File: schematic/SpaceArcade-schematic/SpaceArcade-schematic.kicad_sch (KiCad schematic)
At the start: 4 parts, among them CON1 KY-023, M1 NEMA11

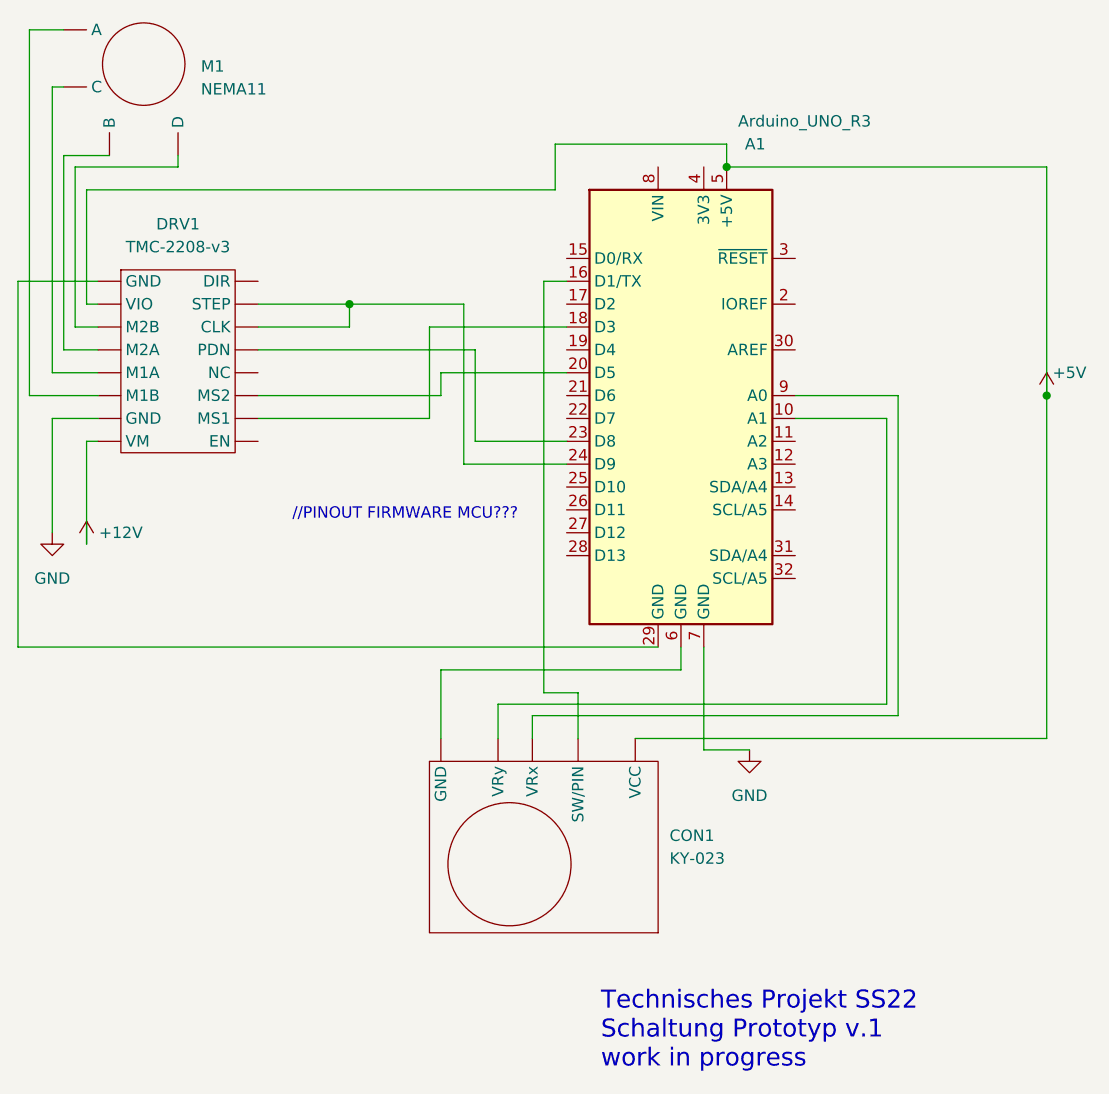
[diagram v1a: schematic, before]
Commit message: Fixing wiring
Fixing driver wiring
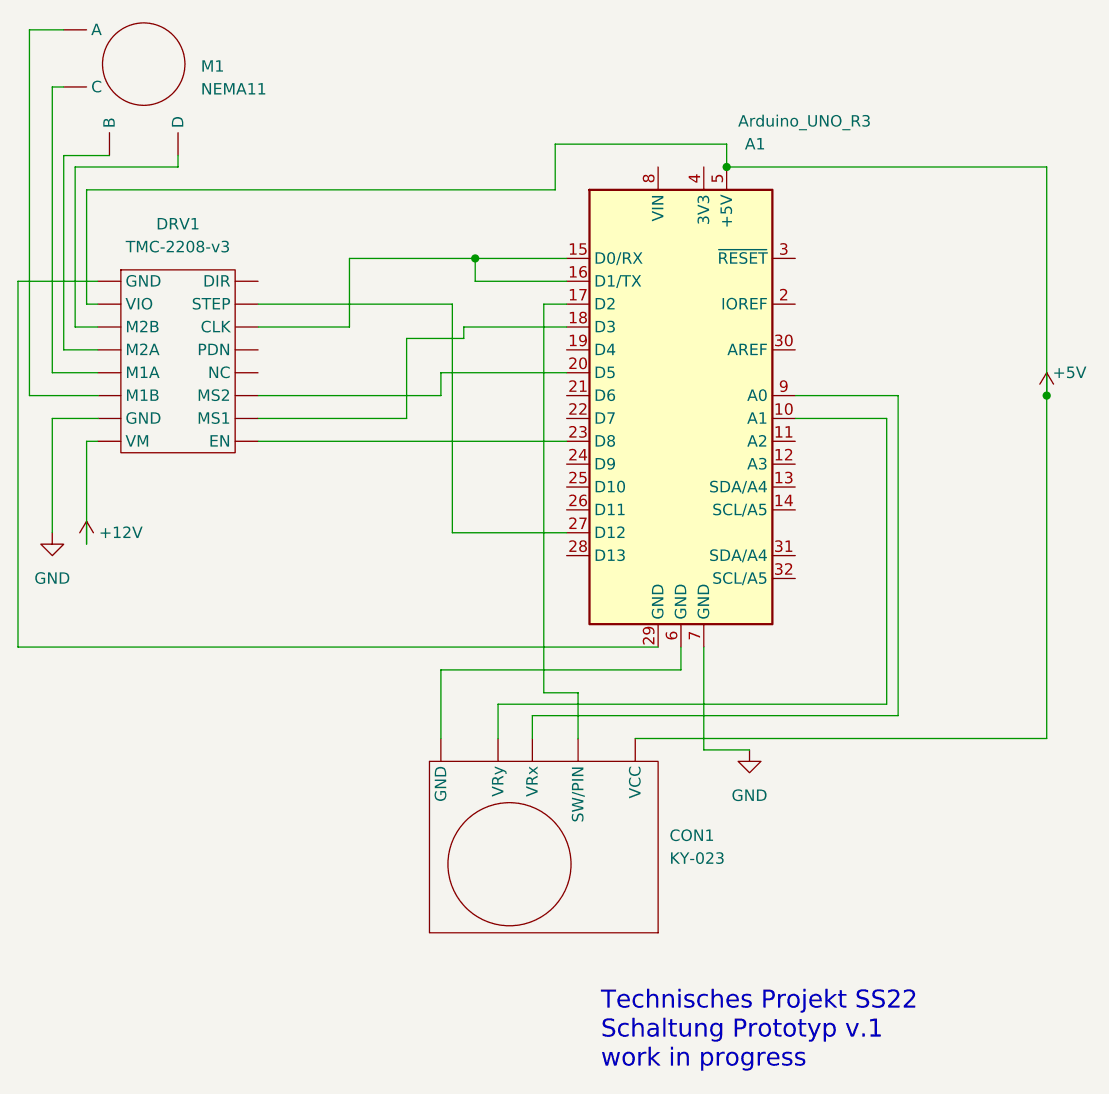
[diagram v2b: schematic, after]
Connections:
- net at A1.24 (D9): no longer DRV1. (VM)
- net at A1.15 (D0/RX): now also A1.16 (D1/TX), DRV1. (VM)
- net at A1.17 (D2): now also CON1. (VRy)
- net at A1.27 (D12): now also DRV1. (VM)
- new net: DRV1. (VM), M1. (D) (x3)
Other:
- note removed: "//PINOUT FIRMWARE MCU???"
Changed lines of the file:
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@@
   (junction (at 194.31 78.74) (diameter 0) (color 255 0 0 1)
   )
-  (junction (at 152.4 93.98) (diameter 0) (color 255 0 255 1)
+  (junction (at 166.37 88.9) (diameter 0) (color 0 0 0 0)
   )
   (junction (at 229.87 104.14) (diameter 0) (color 0 0 0 0)
@@
     (stroke (width 0) (type default) (color 0 0 0 1))
   )
-  (wire (pts (xy 142.24 99.06) (xy 166.37 99.06))
-    (stroke (width 0) (type default) (color 0 255 255 1))
-  )
   (wire (pts (xy 123.19 81.28) (xy 175.26 81.28))
     (stroke (width 0) (type default) (color 255 0 0 1))
@@
   (wire (pts (xy 212.09 106.68) (xy 201.93 106.68))
     (stroke (width 0) (type default) (color 132 0 132 1))
+  )
+  (wire (pts (xy 142.24 93.98) (xy 163.83 93.98))
+    (stroke (width 0) (type default) (color 0 0 0 0))
   )
   (wire (pts (xy 142.24 104.14) (xy 162.56 104.14))
     (stroke (width 0) (type default) (color 0 0 255 1))
   )
+  (wire (pts (xy 142.24 106.68) (xy 158.75 106.68))
+    (stroke (width 0) (type default) (color 0 255 255 1))
+  )
   (wire (pts (xy 120.65 63.5) (xy 116.84 63.5))
     (stroke (width 0) (type default) (color 255 153 0 1))
@@
     (stroke (width 0) (type default) (color 0 132 132 1))
   )
+  (wire (pts (xy 176.53 88.9) (xy 166.37 88.9))
+    (stroke (width 0) (type default) (color 0 0 0 0))
+  )
   (wire (pts (xy 213.36 104.14) (xy 201.93 104.14))
+    (stroke (width 0) (type default) (color 0 255 255 1))
+  )
+  (wire (pts (xy 165.1 97.79) (xy 165.1 96.52))
     (stroke (width 0) (type default) (color 0 255 255 1))
   )
@@
     (stroke (width 0) (type default) (color 0 0 255 1))
   )
-  (wire (pts (xy 152.4 93.98) (xy 142.24 93.98))
-    (stroke (width 0) (type default) (color 255 0 255 1))
+  (wire (pts (xy 165.1 96.52) (xy 176.53 96.52))
+    (stroke (width 0) (type default) (color 0 255 255 1))
   )
   (wire (pts (xy 213.36 139.7) (xy 213.36 104.14))
     (stroke (width 0) (type default) (color 0 255 255 1))
-  )
-  (wire (pts (xy 165.1 93.98) (xy 152.4 93.98))
-    (stroke (width 0) (type default) (color 255 0 255 1))
   )
   (wire (pts (xy 162.56 101.6) (xy 176.53 101.6))
@@
     (stroke (width 0) (type default) (color 255 0 0 1))
   )
+  (wire (pts (xy 176.53 93.98) (xy 173.99 93.98))
+    (stroke (width 0) (type default) (color 255 255 0 1))
+  )
   (wire (pts (xy 115.57 132.08) (xy 186.69 132.08))
     (stroke (width 0) (type default) (color 0 0 0 1))
@@
     (stroke (width 0) (type default) (color 255 0 0 1))
   )
+  (wire (pts (xy 158.75 106.68) (xy 158.75 97.79))
+    (stroke (width 0) (type default) (color 0 255 255 1))
+  )
+  (wire (pts (xy 166.37 88.9) (xy 152.4 88.9))
+    (stroke (width 0) (type default) (color 0 0 0 0))
+  )
+  (wire (pts (xy 166.37 88.9) (xy 166.37 91.44))
+    (stroke (width 0) (type default) (color 0 0 0 0))
+  )
   (wire (pts (xy 115.57 91.44) (xy 124.46 91.44))
     (stroke (width 0) (type default) (color 0 0 0 1))
   )
-  (wire (pts (xy 176.53 111.76) (xy 165.1 111.76))
-    (stroke (width 0) (type default) (color 255 0 255 1))
-  )
-  (wire (pts (xy 165.1 111.76) (xy 165.1 93.98))
-    (stroke (width 0) (type default) (color 255 0 255 1))
+  (wire (pts (xy 152.4 88.9) (xy 152.4 96.52))
+    (stroke (width 0) (type default) (color 0 0 0 0))
   )
   (wire (pts (xy 162.56 134.62) (xy 189.23 134.62))
     (stroke (width 0) (type default) (color 0 0 0 1))
   )
+  (wire (pts (xy 176.53 91.44) (xy 166.37 91.44))
+    (stroke (width 0) (type default) (color 0 0 0 0))
+  )
   (wire (pts (xy 172.72 139.7) (xy 213.36 139.7))
     (stroke (width 0) (type default) (color 0 255 255 1))
   )
+  (wire (pts (xy 152.4 96.52) (xy 142.24 96.52))
+    (stroke (width 0) (type default) (color 0 0 0 0))
+  )
+  (wire (pts (xy 163.83 93.98) (xy 163.83 119.38))
+    (stroke (width 0) (type default) (color 0 0 0 0))
+  )
   (wire (pts (xy 119.38 119.38) (xy 119.38 106.68))
     (stroke (width 0) (type default) (color 0 0 0 1))
+  )
+  (wire (pts (xy 163.83 119.38) (xy 176.53 119.38))
+    (stroke (width 0) (type default) (color 0 0 0 0))
   )
   (wire (pts (xy 124.46 99.06) (xy 120.65 99.06))
@@
     (stroke (width 0) (type default) (color 0 0 0 1))
   )
-  (wire (pts (xy 166.37 99.06) (xy 166.37 109.22))
-    (stroke (width 0) (type default) (color 0 255 255 1))
-  )
-  (wire (pts (xy 166.37 109.22) (xy 176.53 109.22))
-    (stroke (width 0) (type default) (color 0 255 255 1))
-  )
   (wire (pts (xy 120.65 77.47) (xy 120.65 99.06))
     (stroke (width 0) (type default) (color 0 0 0 0))
   )
-  (wire (pts (xy 161.29 96.52) (xy 176.53 96.52))
-    (stroke (width 0) (type default) (color 0 255 0 1))
-  )
-  (wire (pts (xy 142.24 106.68) (xy 161.29 106.68))
-    (stroke (width 0) (type default) (color 0 255 0 1))
-  )
-  (wire (pts (xy 161.29 106.68) (xy 161.29 96.52))
-    (stroke (width 0) (type default) (color 0 255 0 1))
+  (wire (pts (xy 142.24 109.22) (xy 176.53 109.22))
+    (stroke (width 0) (type default) (color 0 0 0 0))
   )
   (wire (pts (xy 121.92 96.52) (xy 121.92 78.74))
@@
     (stroke (width 0) (type default) (color 0 0 0 1))
   )
-  (wire (pts (xy 173.99 91.44) (xy 176.53 91.44))
-    (stroke (width 0) (type default) (color 255 255 0 1))
+  (wire (pts (xy 158.75 97.79) (xy 165.1 97.79))
+    (stroke (width 0) (type default) (color 0 255 255 1))
   )
   (wire (pts (xy 191.77 132.08) (xy 191.77 143.51))
     (stroke (width 0) (type default) (color 0 0 0 1))
   )
-  (wire (pts (xy 142.24 96.52) (xy 152.4 96.52))
-    (stroke (width 0) (type default) (color 255 0 255 1))
-  )
   (wire (pts (xy 175.26 81.28) (xy 175.26 76.2))
     (stroke (width 0) (type default) (color 255 0 0 1))
   )
+  (wire (pts (xy 173.99 93.98) (xy 173.99 137.16))
+    (stroke (width 0) (type default) (color 255 255 0 1))
+  )
   (wire (pts (xy 133.35 78.74) (xy 133.35 77.47))
     (stroke (width 0) (type default) (color 72 72 0 1))
@@
   (wire (pts (xy 123.19 81.28) (xy 123.19 93.98))
     (stroke (width 0) (type default) (color 255 0 0 1))
-  )
-  (wire (pts (xy 152.4 96.52) (xy 152.4 93.98))
-    (stroke (width 0) (type default) (color 255 0 255 1))
   )
   (wire (pts (xy 124.46 93.98) (xy 123.19 93.98))
@@
     (stroke (width 0) (type default) (color 0 132 132 1))
   )
-  (wire (pts (xy 173.99 137.16) (xy 173.99 91.44))
-    (stroke (width 0) (type default) (color 255 255 0 1))
-  )
-  (text "//PINOUT FIRMWARE MCU???" (at 146.05 118.11 0)
-    (effects (font (size 1.27 1.27)) (justify left bottom))
-  )
   (text "Technisches Projekt SS22\nSchaltung Prototyp v.1\nwork in progress"
